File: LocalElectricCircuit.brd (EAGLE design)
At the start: 160 x 100 mm, 53 parts, among them IC1 PIC32MX360F512L, J1 Prog. Port, U1 ADS1118, U2 ADS1118

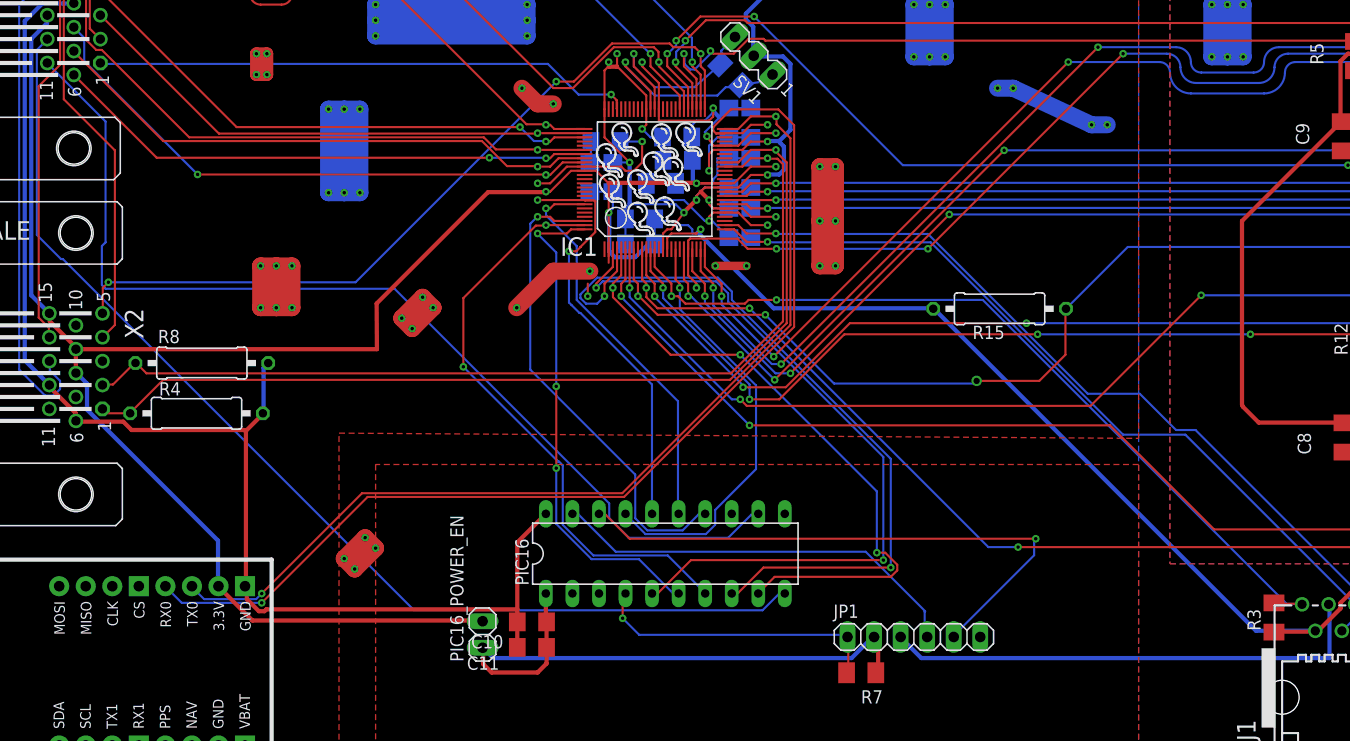
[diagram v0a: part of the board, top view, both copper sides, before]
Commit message: Minor DRC fixes.
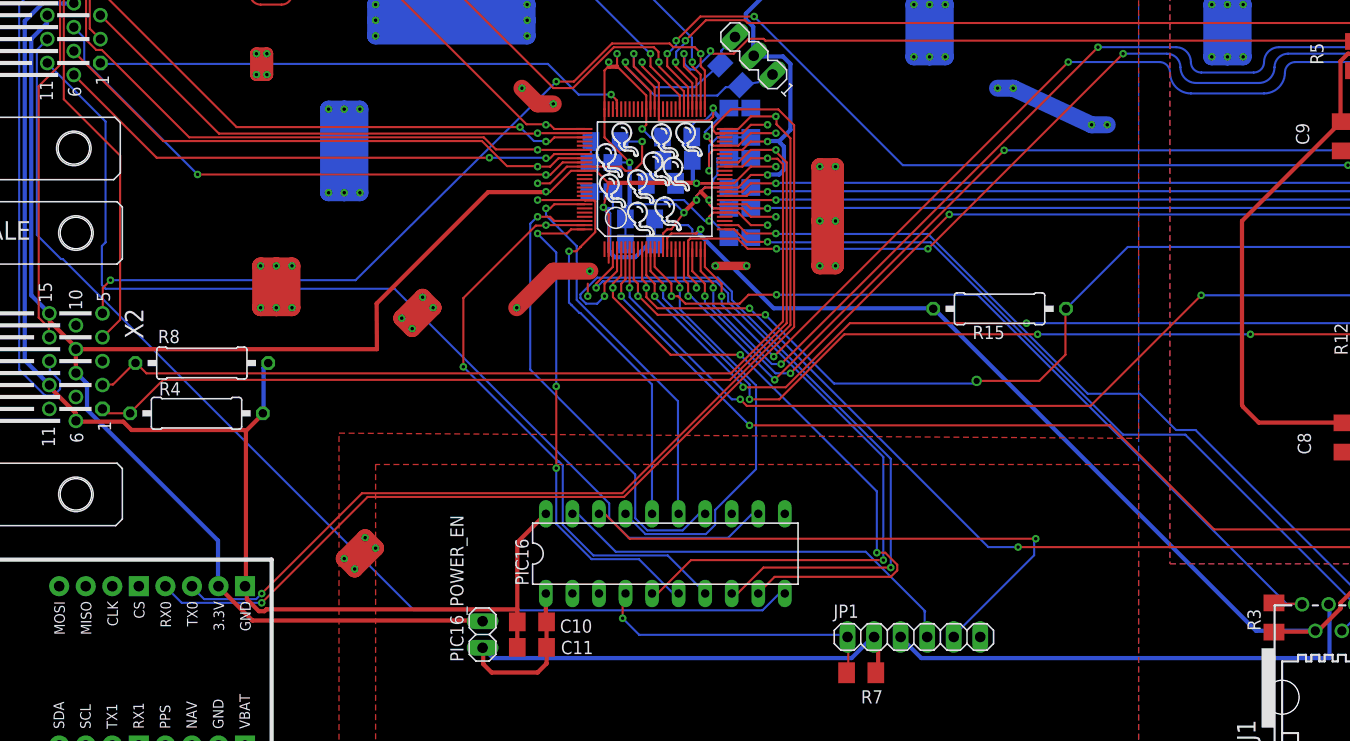
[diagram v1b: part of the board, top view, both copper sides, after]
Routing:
- net +3V3: track 555.2 -> 556.5 mm

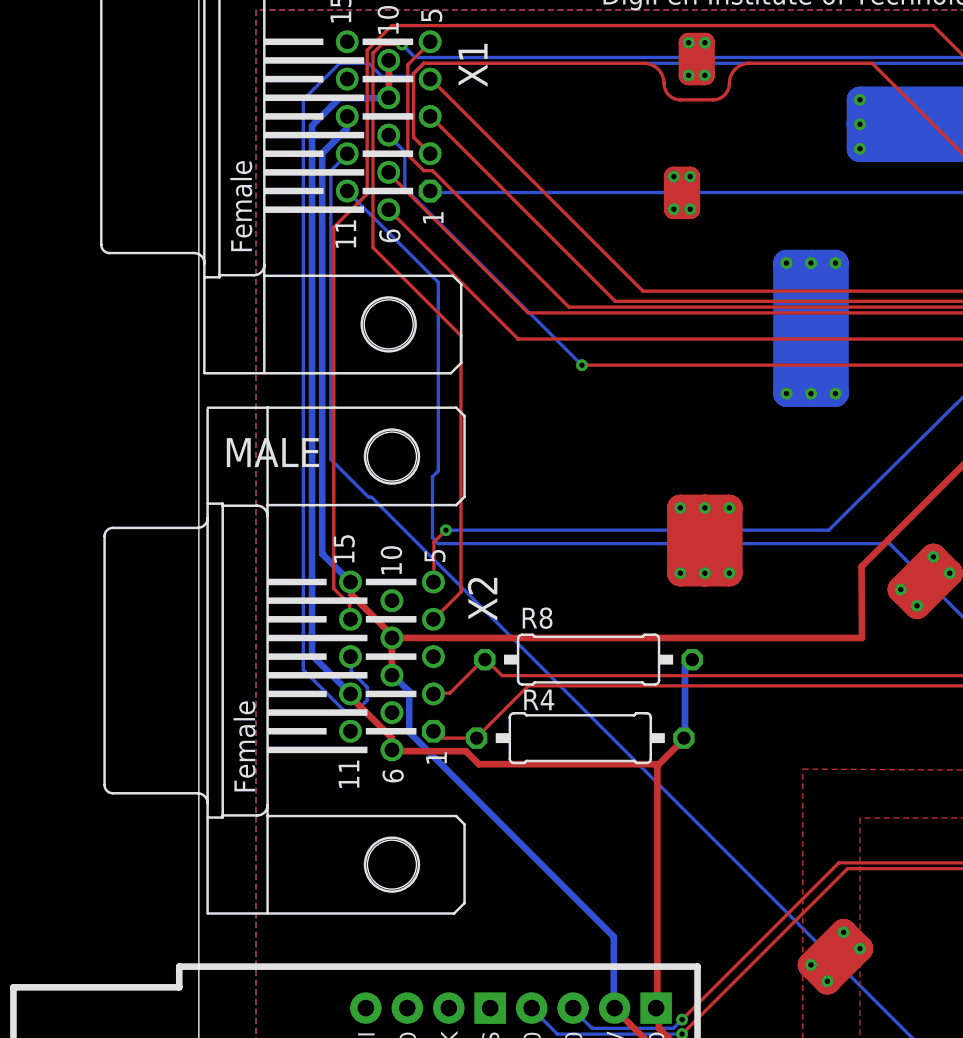
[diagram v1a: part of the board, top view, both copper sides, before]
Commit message: Added Male VGA part
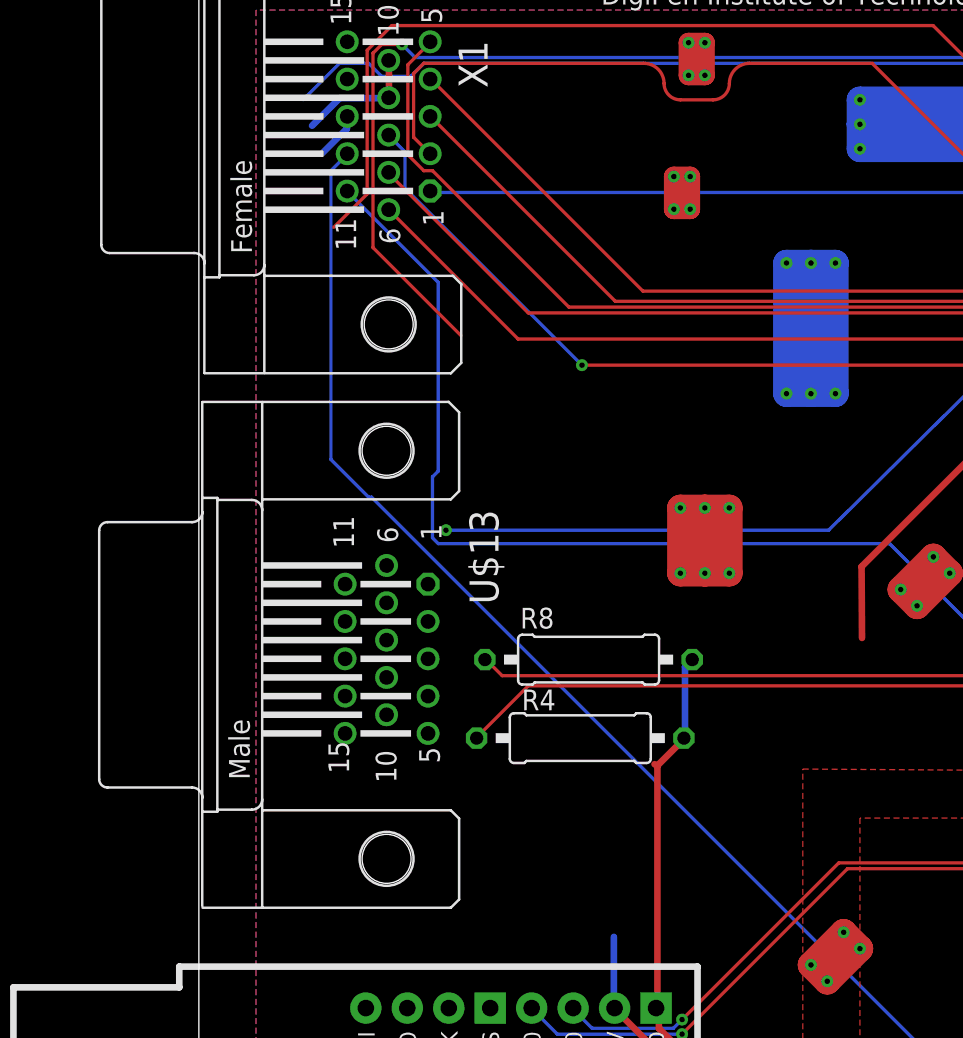
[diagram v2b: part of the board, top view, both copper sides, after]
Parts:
- removed X2: (no value), con-subd:HDF15H
- added U$13: MALE_VGA, MALE_VGA:MALE_PACKAGE
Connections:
- net +3V3: now also U$13.15, U$13.8, U$13.9; no longer X2.15, X2.8, X2.9
- net EXT_TEMP: now also U$13.2; no longer X2.2
- net GND_3V3: now also U$13.12, U$13.6; no longer X2.12, X2.6
- net I2C_SCL: now also U$13.13; no longer X2.13
- net I2C_SDA: now also U$13.14; no longer X2.14
- net RB_TEMP: now also U$13.1; no longer X2.1
- net U1RX: now also U$13.4; no longer X2.4
- net U1TX: now also U$13.5; no longer X2.5
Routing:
- net +3V3: track 556.5 -> 472.2 mm
- net GND_3V3: track 453.1 -> 396.4 mm
- net I2C_SCL: track 114.6 -> 71.3 mm
- net I2C_SDA: track 107.5 -> 83.0 mm
- net U1RX: track 107.8 -> 89.8 mm
- net EXT_TEMP: track 89.6 -> 85.7 mm
- net U1TX: track 75.2 -> 71.7 mm
- net RB_TEMP: track 92.3 -> 89.5 mm
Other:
- board text removed: "MALE"

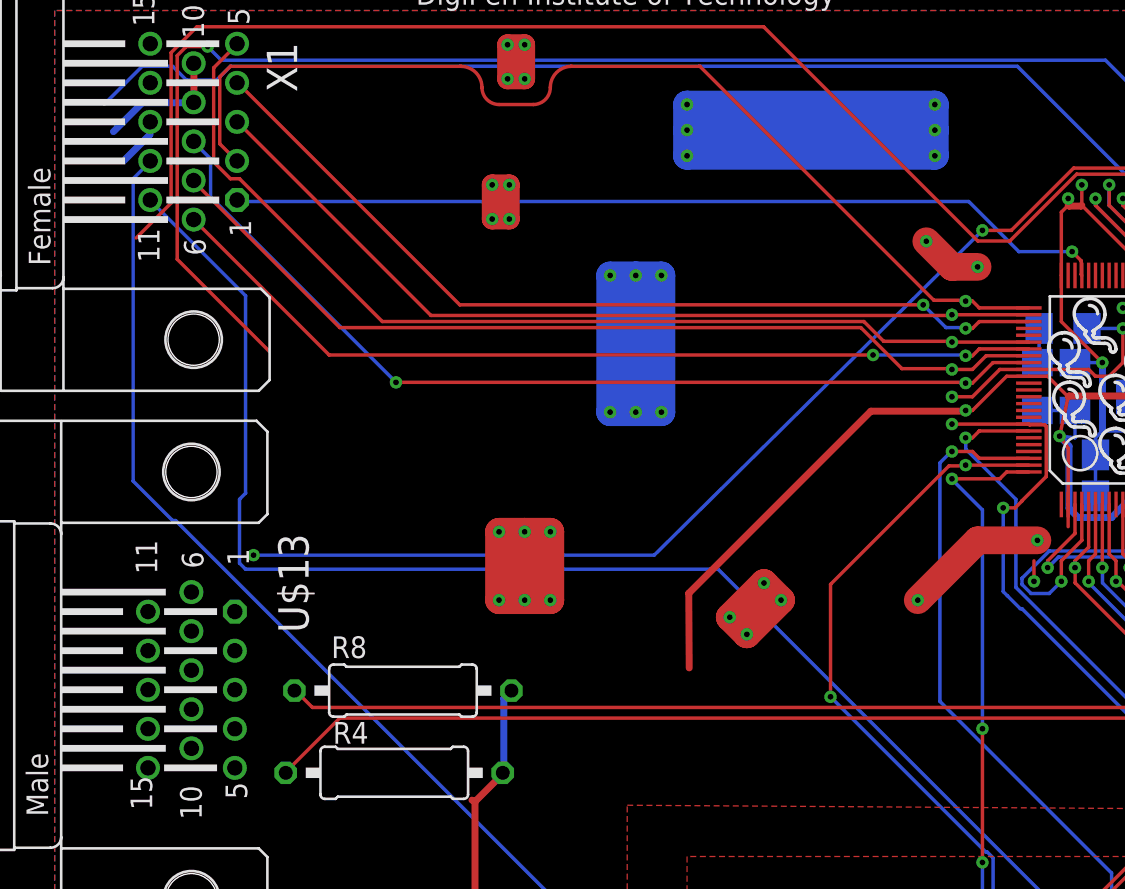
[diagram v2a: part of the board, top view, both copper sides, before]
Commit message: male VGA connector has been auto-routed
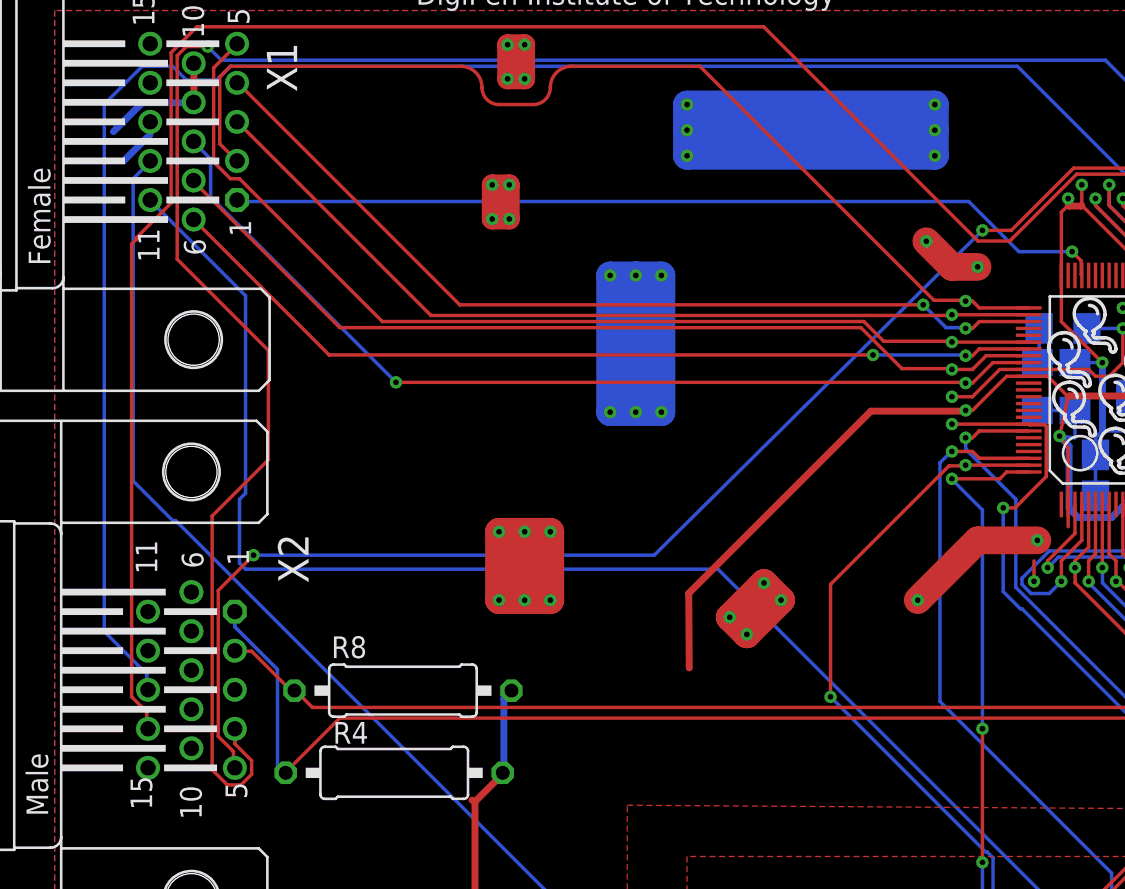
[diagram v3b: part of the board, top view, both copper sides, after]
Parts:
- renumbered U$13 to X2
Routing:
- net I2C_SCL: track 71.3 -> 106.6 mm
- net U1RX: track 89.8 -> 121.6 mm
- net I2C_SDA: track 83.0 -> 112.3 mm
- net U1TX: track 71.7 -> 85.4 mm
- net RB_TEMP: track 89.5 -> 100.2 mm
- net EXT_TEMP: track 85.7 -> 90.2 mm
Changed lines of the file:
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@@
 <element name="U$12" library="Logos" package="BALLOON" value="" x="65.5" y="9.4"/>
 <element name="JP1" library="pinhead" package="1X06" value="" x="92" y="-31"/>
-<element name="U$13" library="MALE_VGA" package="MALE_PACKAGE" value="MALE_VGA" x="11.5" y="-4.5" rot="R270"/>
+<element name="X2" library="MALE_VGA" package="MALE_PACKAGE" value="MALE_VGA" x="11.5" y="-4.5" smashed="yes" rot="R270">
+<attribute name="NAME" x="16.58" y="4.39" size="1.778" layer="25" ratio="10" rot="R270"/>
+<attribute name="VALUE" x="-30.42" y="12.5" size="1.778" layer="27" ratio="10" rot="R270"/>
+</element>
 </elements>
 <signals>
@@
 <wire x1="37.5" y1="19.5" x2="37.5" y2="11.5" width="1.6256" layer="16"/>
 <wire x1="36" y1="19.5" x2="36" y2="11.5" width="1.6256" layer="16"/>
-<contactref element="U$13" pad="9"/>
-<contactref element="U$13" pad="8"/>
-<contactref element="U$13" pad="15"/>
+<contactref element="X2" pad="9"/>
+<contactref element="X2" pad="8"/>
+<contactref element="X2" pad="15"/>
 </signal>
 <signal name="GND_3V3" class="1">
@@
 <wire x1="30.1" y1="22.8" x2="29.1" y2="22.8" width="1.2192" layer="1"/>
 <wire x1="29.1" y1="22.8" x2="29.1" y2="24.8" width="1.2192" layer="1"/>
-<contactref element="U$13" pad="6"/>
-<contactref element="U$13" pad="12"/>
+<contactref element="X2" pad="6"/>
+<contactref element="X2" pad="12"/>
 </signal>
 <signal name="+3V3_PIC_ANALOG">
@@
 <wire x1="10.668" y1="32.3596" x2="11.2014" y2="32.893" width="0.2032" layer="1"/>
 <wire x1="10.668" y1="20.447" x2="10.668" y2="32.3596" width="0.2032" layer="1"/>
-<wire x1="16.0575" y1="15.0575" x2="10.668" y2="20.447" width="0.2032" layer="1"/>
+<wire x1="16.0575" y1="15.0575" x2="16.04645" y2="15.06855" width="0.2032" layer="1"/>
+<wire x1="16.04645" y1="15.06855" x2="10.668" y2="20.447" width="0.2032" layer="1"/>
 <wire x1="70.7644" y1="24.003" x2="70.8" y2="24" width="0.2032" layer="16"/>
 <via x="12.446" y="32.893" extent="1-16" drill="0.3302"/>
-<contactref element="U$13" pad="4"/>
-<wire x1="14.04" y1="-7.029" x2="16.0575" y2="15.0575" width="0" layer="19" extent="1-1"/>
+<contactref element="X2" pad="4"/>
+<wire x1="14.0462" y1="-7.9121" x2="14.0462" y2="-7.112" width="0.2032" layer="1"/>
+<wire x1="15.0241" y1="-8.89" x2="14.0462" y2="-7.9121" width="0.2032" layer="1"/>
+<wire x1="15.0241" y1="-9.6901" x2="15.0241" y2="-8.89" width="0.2032" layer="1"/>
+<wire x1="14.4018" y1="-10.3124" x2="15.0241" y2="-9.6901" width="0.2032" layer="1"/>
+<wire x1="13.6017" y1="-10.3124" x2="14.4018" y2="-10.3124" width="0.2032" layer="1"/>
+<wire x1="12.7127" y1="-9.4234" x2="13.6017" y2="-10.3124" width="0.2032" layer="1"/>
+<wire x1="12.7127" y1="5.4229" x2="12.7127" y2="-9.4234" width="0.2032" layer="1"/>
+<wire x1="16.002" y1="8.7122" x2="12.7127" y2="5.4229" width="0.2032" layer="1"/>
+<wire x1="16.002" y1="15.0241" x2="16.002" y2="8.7122" width="0.2032" layer="1"/>
+<wire x1="14.0462" y1="-7.112" x2="14.04" y2="-7.029" width="0.2032" layer="1"/>
+<wire x1="16.002" y1="15.0241" x2="16.04645" y2="15.06855" width="0.2032" layer="1"/>
 </signal>
 <signal name="U1TX">
@@
 <via x="15.1352" y="3.1337" extent="1-16" drill="0.3302"/>
 <via x="57.785" y="22.1361" extent="1-16" drill="0.3302"/>
-<contactref element="U$13" pad="5"/>
-<wire x1="14.04" y1="-9.315" x2="15.1352" y2="3.1337" width="0" layer="19" extent="16-16"/>
+<contactref element="X2" pad="5"/>
+<wire x1="13.9573" y1="-8.3566" x2="13.9573" y2="-9.2456" width="0.2032" layer="1"/>
+<wire x1="13.0683" y1="-7.4676" x2="13.9573" y2="-8.3566" width="0.2032" layer="1"/>
+<wire x1="13.0683" y1="1.0668" x2="13.0683" y2="-7.4676" width="0.2032" layer="1"/>
+<wire x1="15.1352" y1="3.1337" x2="13.0683" y2="1.0668" width="0.2032" layer="1"/>
+<wire x1="13.9573" y1="-9.2456" x2="14.04" y2="-9.315" width="0.2032" layer="1"/>
 </signal>
 <signal name="GND_5V" class="1">
@@
 <wire x1="60.5409" y1="10.7569" x2="60.5" y2="10.8" width="0.2032" layer="1"/>
 <wire x1="60.0964" y1="0" x2="60" y2="0" width="0.2032" layer="16"/>
-<wire x1="60" y1="0" x2="59.25" y2="0.75" width="0.2032" layer="16"/>
+<wire x1="60" y1="0" x2="59" y2="1" width="0.2032" layer="16"/>
 <wire x1="60.0964" y1="6.3119" x2="60.0964" y2="6.2964" width="0.2032" layer="1"/>
 <wire x1="60.0964" y1="6.2964" x2="59.7" y2="5.9" width="0.2032" layer="1"/>
@@
 <via x="59" y="5.9" extent="1-16" drill="0.3302"/>
 <wire x1="59" y1="5.9" x2="59" y2="1" width="0.2032" layer="16"/>
-<wire x1="59" y1="1" x2="59.25" y2="0.75" width="0.2032" layer="16"/>
 </signal>
 <signal name="PBUS1">
@@
 <wire x1="17.6022" y1="-4.8006" x2="17.526" y2="-4.794" width="0.2032" layer="1"/>
 <wire x1="17.4244" y1="-4.8006" x2="17.526" y2="-4.794" width="0.2032" layer="1"/>
-<contactref element="U$13" pad="2"/>
-<wire x1="14.04" y1="-2.457" x2="17.4244" y2="-4.8006" width="0" layer="19" extent="1-1"/>
+<contactref element="X2" pad="2"/>
+<wire x1="15.0241" y1="-2.4892" x2="14.0462" y2="-2.4892" width="0.2032" layer="1"/>
+<wire x1="17.3355" y1="-4.8006" x2="15.0241" y2="-2.4892" width="0.2032" layer="1"/>
+<wire x1="14.0462" y1="-2.4892" x2="14.04" y2="-2.457" width="0.2032" layer="1"/>
+<wire x1="17.3355" y1="-4.8006" x2="17.526" y2="-4.794" width="0.2032" layer="1"/>
 </signal>
 <signal name="RB_TEMP">
@@
 <wire x1="78.8543" y1="15.5575" x2="78.8" y2="15.6" width="0.2032" layer="1"/>
 <wire x1="17.0688" y1="-9.5123" x2="17.018" y2="-9.604" width="0.2032" layer="1"/>
-<contactref element="U$13" pad="1"/>
-<wire x1="20.1803" y1="-6.4008" x2="14.04" y2="-0.171" width="0" layer="19" extent="1-1"/>
+<contactref element="X2" pad="1"/>
+<wire x1="14.0462" y1="-1.0668" x2="14.0462" y2="-0.1778" width="0.2032" layer="16"/>
+<wire x1="16.5354" y1="-3.556" x2="14.0462" y2="-1.0668" width="0.2032" layer="16"/>
+<wire x1="16.5354" y1="-9.1567" x2="16.5354" y2="-3.556" width="0.2032" layer="16"/>
+<wire x1="16.9799" y1="-9.6012" x2="16.5354" y2="-9.1567" width="0.2032" layer="16"/>
+<wire x1="14.0462" y1="-0.1778" x2="14.04" y2="-0.171" width="0.2032" layer="16"/>
+<wire x1="16.9799" y1="-9.6012" x2="17.018" y2="-9.604" width="0.2032" layer="16"/>
 </signal>
 <signal name="BALLS2">
@@
 <wire x1="66.7639" y1="24.8031" x2="59.8297" y2="31.7373" width="0.2032" layer="16"/>
 <wire x1="66.7639" y1="24.8031" x2="66.8" y2="24.8" width="0.2032" layer="16"/>
-<contactref element="U$13" pad="13"/>
-<wire x1="8.96" y1="-4.743" x2="6.4008" y2="29.5148" width="0" layer="19" extent="16-16"/>
+<contactref element="X2" pad="13"/>
+<wire x1="8.89" y1="-3.8227" x2="8.89" y2="-4.7117" width="0.2032" layer="16"/>
+<wire x1="6.4008" y1="-1.3335" x2="8.89" y2="-3.8227" width="0.2032" layer="16"/>
+<wire x1="6.4008" y1="29.5148" x2="6.4008" y2="-1.3335" width="0.2032" layer="16"/>
+<wire x1="8.89" y1="-4.7117" x2="8.96" y2="-4.743" width="0.2032" layer="16"/>
 </signal>
 <signal name="I2C_SDA">
@@
 <wire x1="67.564" y1="24.0919" x2="67.564" y2="24.9809" width="0.2032" layer="1"/>
 <wire x1="67.564" y1="24.0919" x2="67.6" y2="24" width="0.2032" layer="1"/>
-<contactref element="U$13" pad="14"/>
-<wire x1="8.96" y1="-7.029" x2="8.2677" y2="21.6916" width="0" layer="19" extent="1-1"/>
+<contactref element="X2" pad="14"/>
+<wire x1="8.89" y1="-6.0452" x2="8.89" y2="-7.0231" width="0.2032" layer="1"/>
+<wire x1="8.001" y1="-5.1562" x2="8.89" y2="-6.0452" width="0.2032" layer="1"/>
+<wire x1="8.001" y1="21.336" x2="8.001" y2="-5.1562" width="0.2032" layer="1"/>
+<wire x1="8.2677" y1="21.6027" x2="8.001" y2="21.336" width="0.2032" layer="1"/>
+<wire x1="8.89" y1="-7.0231" x2="8.96" y2="-7.029" width="0.2032" layer="1"/>
+<wire x1="8.2677" y1="21.6027" x2="8.2677" y2="21.6916" width="0.2032" layer="1"/>
 </signal>
 <signal name="CONDUCTIVITY_ENABLE">
